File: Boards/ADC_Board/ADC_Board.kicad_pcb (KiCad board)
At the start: 4 copper layers, 100 x 50 mm, 156 parts, among them J1 SWD JST PH, J10 I2CC JST, J11 DB9 Microfit, J12 Backup Power, J13 Load Cell A, J14 Load Cell B, J15 MIPA_A, J16 Load Cell C, J17 MIPA_B, J18 Thermocouple A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

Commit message: Nearing complete layout on both boards
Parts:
- added R51: 10K, Resistor_SMD:R_0603_1608Metric, F.Cu at (187.6, 95.0)
- added R52: 10K, Resistor_SMD:R_0603_1608Metric, F.Cu at (163.8, 72.4)
- added R53: 10K, Resistor_SMD:R_0603_1608Metric, F.Cu at (150.6, 76.2)
- added R54: 10K, Resistor_SMD:R_0603_1608Metric, F.Cu at (187.6, 89.4)
- added R55: 10K, Resistor_SMD:R_0603_1608Metric, F.Cu at (159.8, 76.0)
- added R56: 10K, Resistor_SMD:R_0603_1608Metric, F.Cu at (145.0, 76.2)
- D1, D5, D6, D7, J10, J15, J17, J19, J22, J5, J7: moved to B.Cu
- TP1, TP10, TP11, TP12, TP13, TP14, TP15, TP16, TP17, TP18, TP2, TP3, TP4, TP5, TP6, TP7, TP8, TP9: footprint TestPoint:TestPoint_Pad_1.5x1.5mm -> TestPoint:TestPoint_Pad_D1.0mm
- moved J5 171.4 mm to (185.7, 88.2), turned to -90 degrees
- moved J7 146.9 mm to (157.0, 74.2)
- moved R13 145.1 mm to (181.2, 110.9), turned to -90 degrees
- moved R15 139.4 mm to (175.5, 118.1)
- moved R14 139.4 mm to (175.5, 115.3)
- moved J10 136.3 mm to (143.8, 74.2)
- moved C4 133.5 mm to (159.6, 83.6)
- moved C3 130.1 mm to (156.2, 81.6)
- moved D7 129.9 mm to (177.8, 117.0)
- moved D6 129.8 mm to (177.8, 114.2)
- moved D5 129.8 mm to (177.8, 111.4)
- moved C43 123.7 mm to (137.0, 72.8), turned to -90 degrees
- moved C36 123.5 mm to (137.0, 83.0), turned to 90 degrees
- moved R35 121.7 mm to (134.6, 78.2)
- moved TP20 120.4 mm to (186.2, 83.1), turned to 90 degrees
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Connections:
- D1 pad 1: /I2C3_SDA -> /I2C1_SDA
- D1 pad 3: /I2C3_SCL -> /I2C1_SCL
- D2 pad 1: /I2C1_SDA -> /I2C3_SDA
- D2 pad 3: /I2C1_SCL -> /I2C3_SCL
- J11 pad 3: /CAN2_AUX -> unconnected-(J11-Pad3)
- J15 pad 3: +5V -> +5VA
- J17 pad 3: +5V -> +5VA
- J19 pad 3: +5V -> +5VA
- J6 pad 3: /CAN1_AUX -> unconnected-(J6-Pad3)
- U1 pad 61: /CAN2_AUX -> unconnected-(U1-PB7-Pad61)
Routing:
- net +5V: track 17.0 -> 180.3 mm, vias 0 -> 5
- net /I2C1_SCL: track 0.00 -> 52.9 mm, vias 0 -> 1
- net +3V3: track 15.7 -> 66.9 mm, vias 0 -> 13
- net /I2C1_SDA: track 0.00 -> 42.6 mm, vias 0 -> 1
- net GND: track 44.1 -> 82.4 mm, vias 23 -> 69
- net /LED2: track 0.00 -> 30.2 mm
- net /I2C2_SCL: track 0.00 -> 29.3 mm
- net /LED1: track 0.00 -> 28.9 mm
- net /CAN1_TX: track 0.00 -> 28.7 mm
- net /CAN1_RX: track 0.00 -> 26.4 mm
- net /2S+ A10: track 1.56 -> 27.7 mm, vias 0 -> 2
- net /I2C3_SDA: track 0.00 -> 25.6 mm
- net /I2C2_SDA: track 0.00 -> 23.5 mm
- net /CJT A0: track 0.00 -> 23.4 mm
- net +7V4: track 18.5 -> 41.4 mm
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- added copper zone on In2.Cu, net +3V3
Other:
- board text added: "7V4"
- board text added: "BACKUP PWR"
- board text added: "CAN IN"
- board text added: "CAN OUT"
- board text added: "CJT"
- board text added: "ERR"
- board text added: "EXTRAS"
- board text added: "I^{2}C A"
- board text added: "I^{2}C B"
- board text added: "I^{2}C C"
- board text added: "LOAD A"
- board text added: "LOAD B"
- board text added: "LOAD C"
- board text added: "MIPA A"
- board text added: "MIPA B"
- board text added: "MIPA C"
- board text added: "ST"
- board text added: "SWD"
- board text added: "TERM A"
- board text added: "TERM B"
- board text added: "THERMO A"
- board text added: "THERMO B"
- board text added: "THERMO C"
- board text added: "UART"

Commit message: Completed with manufacturing files
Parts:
- added G***: LOGO, logo:uca_logo2, B.Cu at (149.8, 88.6)
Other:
- board text added: "${CURRENT_DATE}"
- board text added: "${REVISION}"
- board text added: "B Redpath"
- board text added: "Date"
- board text added: "Drawn"
- board text added: "HYBRID ADC ECU"
- board text added: "Revision"

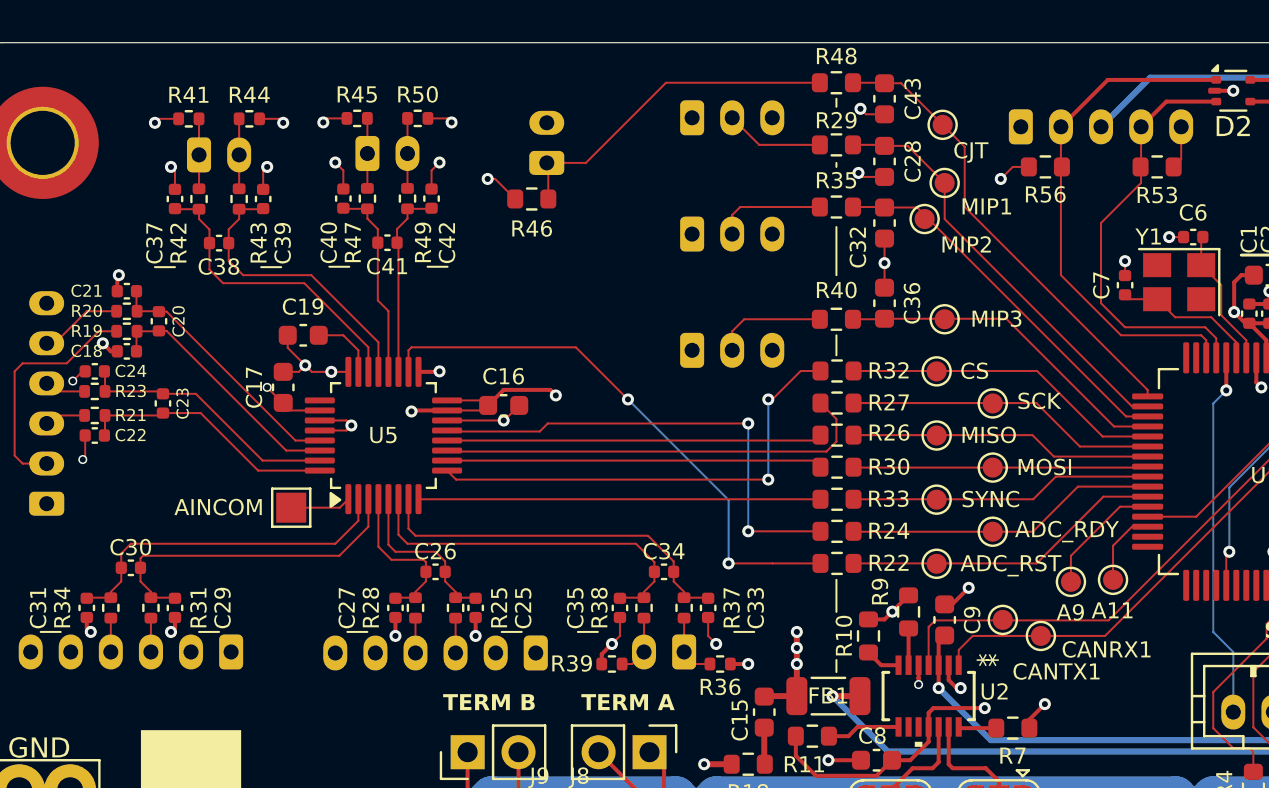
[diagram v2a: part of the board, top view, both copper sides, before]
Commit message: Rev B ADC Board
Change ADC to QFN due to order error
Adds voltage divider to MIPA ADC lines
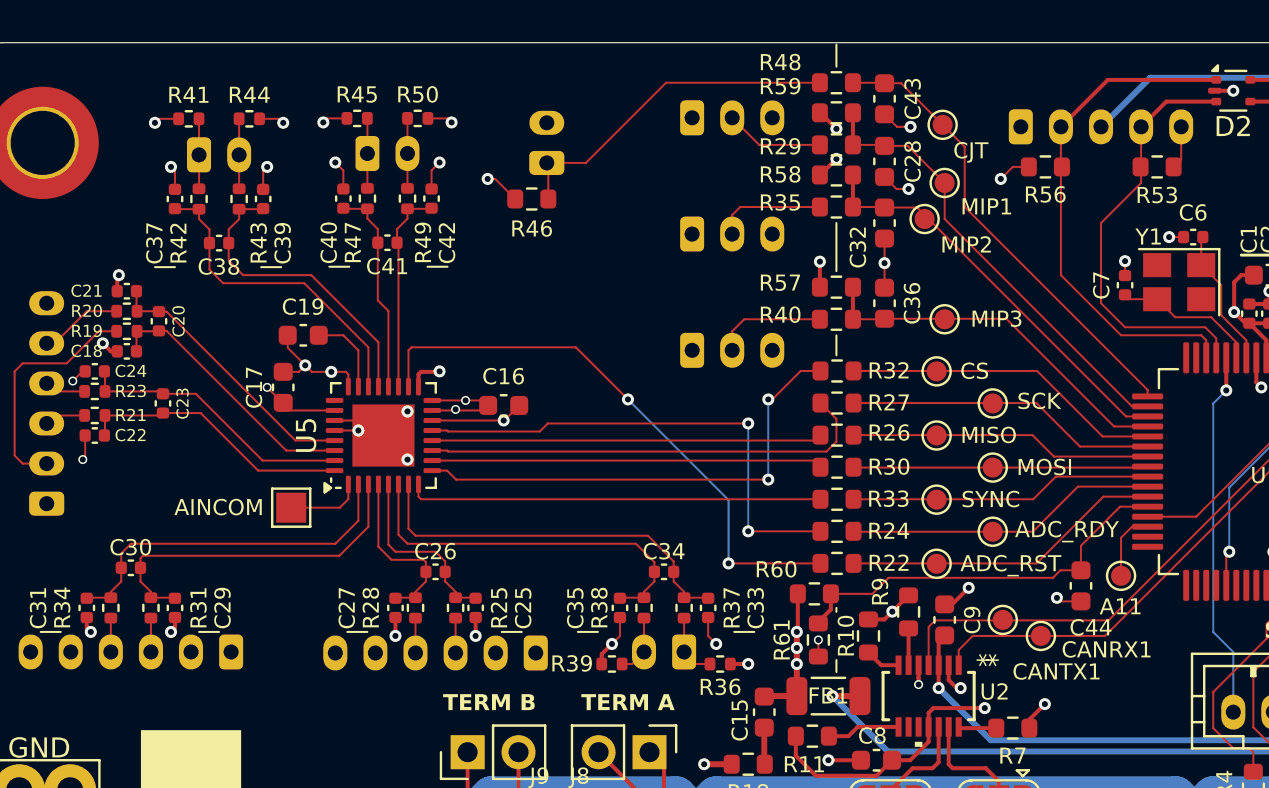
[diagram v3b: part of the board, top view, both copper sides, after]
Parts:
- removed TP12: A9, TestPoint:TestPoint_Pad_D1.0mm
- added C44: 100n, Capacitor_SMD:C_0603_1608Metric, F.Cu at (146.8, 97.1)
- added R57: 5K90, Resistor_SMD:R_0603_1608Metric, F.Cu at (134.6, 82.2)
- added R58: 5K90, Resistor_SMD:R_0603_1608Metric, F.Cu at (134.6, 76.6)
- added R59: 5K90, Resistor_SMD:R_0603_1608Metric, F.Cu at (134.6, 73.5)
- added R60: 3K, Resistor_SMD:R_0603_1608Metric, F.Cu at (133.5, 97.5)
- added R61: 5K90, Resistor_SMD:R_0603_1608Metric, F.Cu at (133.7, 99.8)
- R29, R35, R40: value 2K -> 3K
- U5: footprint Package_QFP:LQFP-32_5x5mm_P0.5mm -> Package_DFN_QFN:QFN-32-1EP_5x5mm_P0.5mm_EP3.1x3.1mm
- moved TP15 0.45 mm to (148.8, 96.6)
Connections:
- U1 pad 28: /A9 -> /5VREF
- U1 pad 64: /CAN1_AUX -> unconnected-(U1-PC10-Pad64)
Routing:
- net /5VREF: track 0.00 -> 20.1 mm
- net GND: track 82.4 -> 90.3 mm, vias 69 -> 76
- net /A9: track 6.14 -> 0.00 mm
- net +3V3: track 66.9 -> 62.8 mm
- net +5VA: track 13.1 -> 15.8 mm
- net /MIPA_B A2: track 19.2 -> 20.8 mm
- net /MIPA_C A3: track 16.9 -> 18.5 mm
- net /MIPA_A A1: track 21.2 -> 22.8 mm
- net Net-(U5-AIN1): track 18.3 -> 19.0 mm
- net Net-(U5-AIN3): track 8.06 -> 8.80 mm
- net Net-(U5-AIN2): track 8.49 -> 9.22 mm
- net Net-(U5-AINCOM): track 3.03 -> 3.76 mm
- net Net-(U5-AIN5): track 17.2 -> 18.0 mm
- net Net-(U5-AIN0): track 18.6 -> 19.4 mm
- net Net-(U5-AIN4): track 16.8 -> 17.5 mm
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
